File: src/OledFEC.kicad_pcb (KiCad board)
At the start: 2 copper layers, 24 x 27.9 mm, 14 parts, among them J1 105444-0001, J2 B4B-XH-A, U1 16F1454, U2 MIC2005A-1

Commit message: Using MIC2091-1 instead of MIC2005A-1
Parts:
- U2: footprint Medo64:U LoadSwitch 500mA [MIC2005A-1] (SOT23-5) -> Medo64:U LoadSwitch 100mA [MIC2091-1] (SOT23-5)
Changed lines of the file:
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@@
 		)
 	)
-	(footprint "Medo64:U LoadSwitch 500mA [MIC2005A-1] (SOT23-5)"
+	(footprint "Medo64:U LoadSwitch 100mA [MIC2091-1] (SOT23-5)"
 		(layer "F.Cu")
 		(at 28.2 36 -90)
 		(tags "SOT95P240X110-3N")
 		(property "Reference" "U2"
-			(at -2.8 0 0)
+			(at 0 -2.2 -90)
 			(layer "F.SilkS")
 			(effects
@@
 			)
 		)
-		(property "Footprint" "Medo64:U LoadSwitch 500mA [MIC2005A-1] (SOT23-5)"
-			(at 0 0 90)
+		(property "Footprint" "Medo64:U LoadSwitch 100mA [MIC2091-1] (SOT23-5)"
+			(at 0 0 -90)
 			(layer "F.Fab")
 			(hide yes)
@@
 		)
 		(property "Datasheet" ""
-			(at 0 0 90)
+			(at 0 0 -90)
 			(layer "F.Fab")
 			(hide yes)
@@
 		)
 		(property "Description" ""
-			(at 0 0 90)
+			(at 0 0 -90)
 			(layer "F.Fab")
 			(hide yes)
@@
 			(layer "F.Fab")
 		)
-		(fp_text user "~{FAULT}"
-			(at 0.7 0.95 90)
+		(fp_text user "EN"
+			(at -0.7 0.95 -90)
+			(layer "Cmts.User" knockout)
+			(effects
+				(font
+					(size 0.13 0.07)
+					(thickness 0.01)
+					(bold yes)
+				)
+				(justify left)
+			)
+		)
+		(fp_text user "IN"
+			(at -0.7 -0.95 -90)
+			(layer "Cmts.User" knockout)
+			(effects
+				(font
+					(size 0.13 0.07)
+					(thickness 0.01)
+					(bold yes)
+				)
+				(justify left)
+			)
+		)
+		(fp_text user "GND"
+			(at -0.7 0 -90)
 			(layer "Cmts.User" knockout)
 			(effects
@@
 		)
 		(fp_text user "OUT"
-			(at 0.7 -0.95 90)
-			(layer "Cmts.User" knockout)
-			(effects
-				(font
-					(size 0.13 0.07)
-					(thickness 0.01)
-					(bold yes)
-				)
-				(justify left)
-			)
-		)
-		(fp_text user "IN"
-			(at -0.7 -0.95 90)
+			(at 0.7 -0.95 -90)
 			(layer "Cmts.User" knockout)
 			(effects
@@
 			)
 		)
-		(fp_text user "EN"
-			(at -0.7 0.95 90)
+		(fp_text user "~{FAULT}"
+			(at 0.7 0.95 -90)
 			(layer "Cmts.User" knockout)
 			(effects
-				(font
-					(size 0.13 0.07)
-					(thickness 0.01)
-					(bold yes)
-				)
-				(justify right)
-			)
-		)
-		(fp_text user "GND"
-			(at -0.7 0 90)
-			(layer "Cmts.User" knockout)
-			(effects

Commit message: Cleanup
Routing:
- net 5V: track 47.6 -> 47.0 mm
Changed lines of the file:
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@@
-	)
-	(segment
-		(start 28.2 40.75)
-		(end 28.25 40.8)
-		(width 0.2)
-		(layer "F.Cu")
-		(net 4)
 	)
 	(segment
@@
 	)
 	(segment
-		(start 31.025 32.375)
-		(end 31.025 31.9)
-		(width 0.2)
-		(layer "F.Cu")
-		(net 6)
-	)
-	(segment
 		(start 29.15 33.65)
 		(end 29.15 34.75)
@@
 		(net 6)
 	)
-	(segment
-		(start 31.35 34.75)
-		(end 31.4 34.8)
-		(width 0.2)
-		(layer "F.Cu")
-		(net 6)
-	)
 	(via
 		(at 29.8 29.9)
@@
 		(width 0.2)
 		(layer "F.Cu")
-		(net 13)
-	)
-	(segment
-		(start 29.15 37.35)
-		(end 29.15 37.25)
-		(width 0.2)
-		(layer "F.Cu")

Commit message: Added pull-up jumper
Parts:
- added JP1: Jumper, Medo64:JP Dual (1205), F.Cu at (39.7, 44.9)
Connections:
- R3 pad 2: 3V3 -> PULL_UP
- R4 pad 2: 3V3 -> PULL_UP
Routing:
- net PULL_UP: track 0.00 -> 20.9 mm, vias 0 -> 3
- net 5V: track 47.0 -> 64.8 mm
- net OLED_SCL: track 32.1 -> 23.4 mm, vias 1 -> 2
- net 3V3: track 28.1 -> 34.3 mm, vias 5 -> 4
- net GND: track 82.7 -> 87.8 mm, vias 4 -> 5
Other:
- board text added: "3V3"
- board text added: "5V"

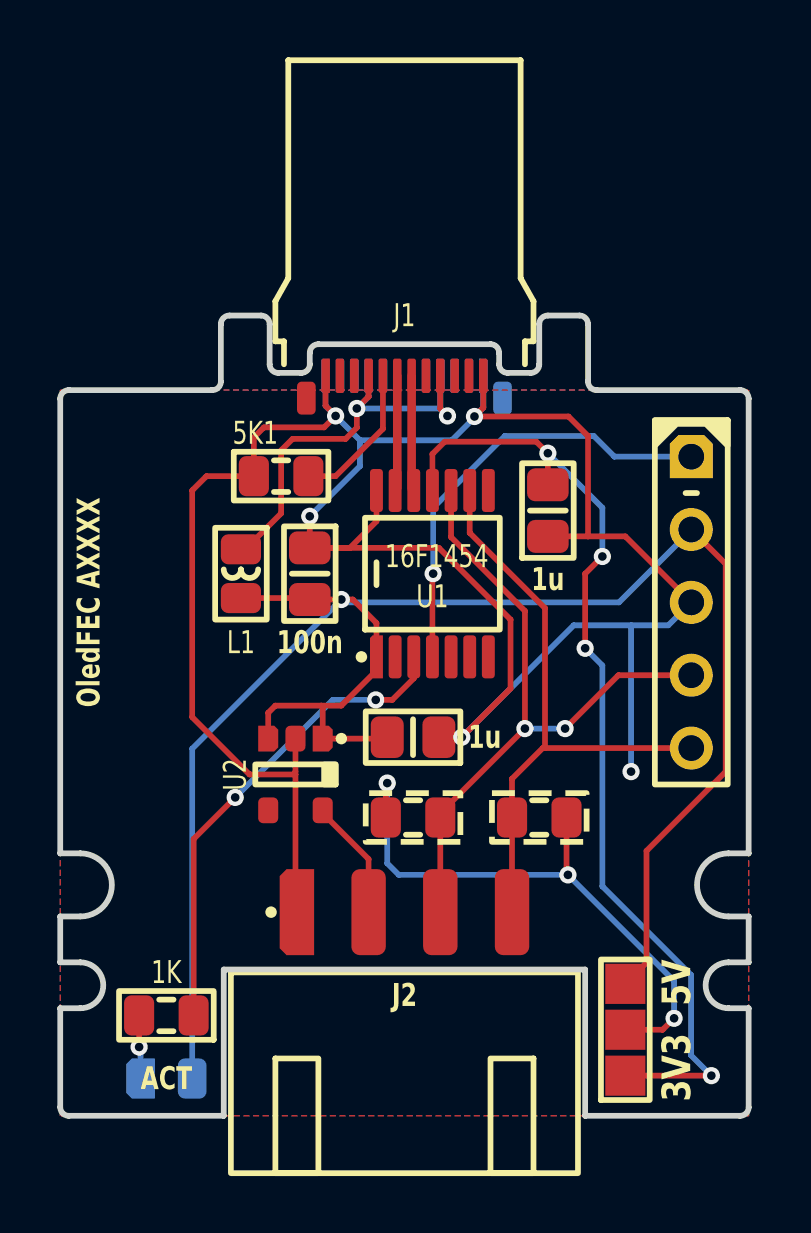
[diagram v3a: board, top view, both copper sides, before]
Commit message: Updated pull-up resistors to be populated
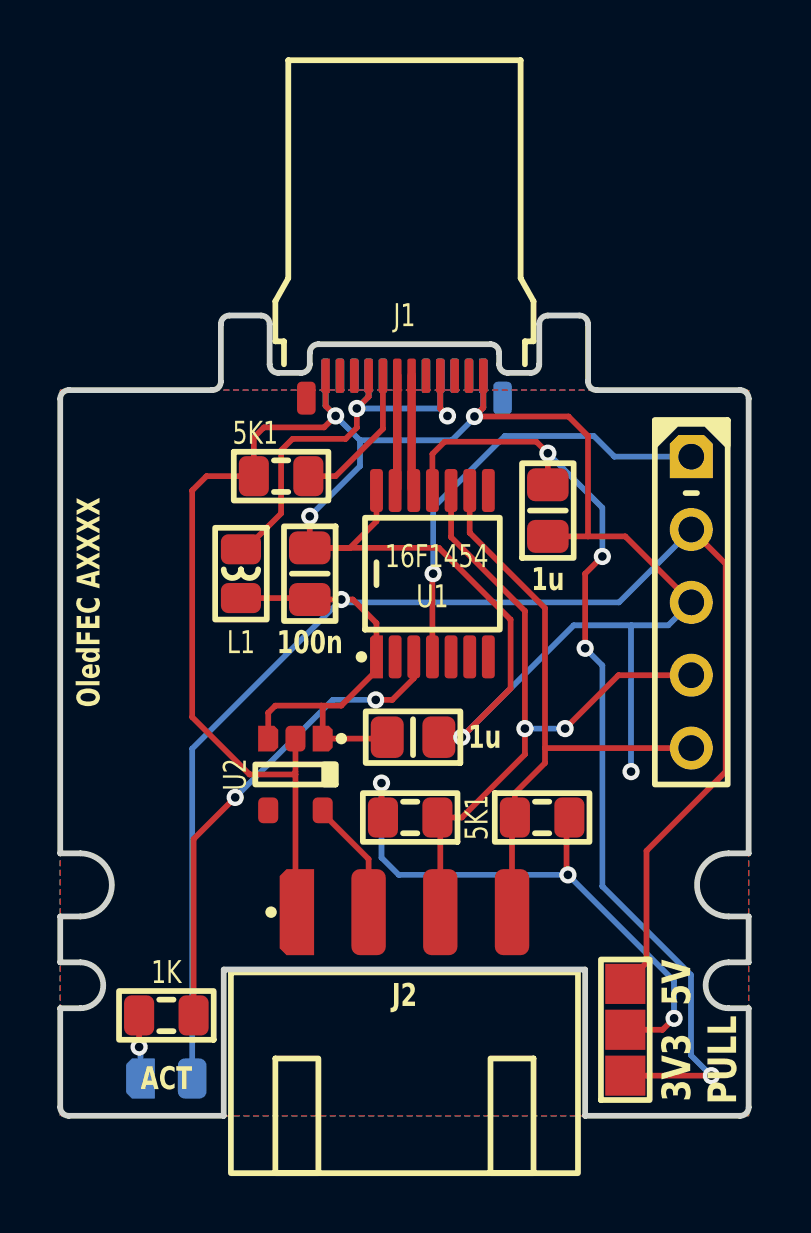
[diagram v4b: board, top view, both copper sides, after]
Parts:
- R3, R4: footprint Medo64:R Optional (0805) -> Medo64:R (0805)
- moved R3 0.10 mm to (32.2, 37.5)
- moved R4 0.10 mm to (36.8, 37.5)
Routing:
- net OLED_SCL: track 23.4 -> 24.1 mm
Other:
- board text added: "PULL"
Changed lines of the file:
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@@
 		)
 	)
-	(footprint "Medo64:R Optional (0805)"
+	(footprint "Medo64:R (0805)"
 		(layer "F.Cu")
-		(at 36.7 37.5)
+		(at 36.8 37.5)
 		(tags "RESC2013X70N")
 		(property "Reference" "R4"
@@
 			)
 		)
-		(property "Footprint" "Medo64:R Optional (0805)"
+		(property "Footprint" "Medo64:R (0805)"
 			(at 0 0 0)
-			(layer "B.Fab")
+			(layer "F.Fab")
 			(hide yes)
 			(effects
@@
 					(thickness 0.15)
 				)
-				(justify mirror)
 			)
 		)
 		(property "Datasheet" ""
 			(at 0 0 0)
-			(layer "B.Fab")
+			(layer "F.Fab")
 			(hide yes)
 			(effects
@@
 					(thickness 0.15)
 				)
-				(justify mirror)
 			)
 		)
 		(property "Description" ""
 			(at 0 0 0)
-			(layer "B.Fab")
+			(layer "F.Fab")
 			(hide yes)
 			(effects
@@
 					(thickness 0.15)
 				)
-				(justify mirror)
 			)
 		)
-		(attr smd exclude_from_bom)
+		(attr smd)
 		(fp_line
-			(start -0.25 -0.6)
-			(end 0.25 -0.6)
+			(start -0.25 -0.55)
+			(end 0.25 -0.55)
 			(stroke
 				(width 0.2)
@@
 		)
 		(fp_line
-			(start -0.25 0.6)
-			(end 0.25 0.6)
+			(start -0.25 0.55)
+			(end 0.25 0.55)
 			(stroke
 				(width 0.2)
@@
 			(stroke
 				(width 0.2)
-				(type dash)
+				(type default)
 			)
 			(fill none)
@@
 			(at -0.95 0)
 			(size 1.05 1.4)
-			(layers "F.Cu" "F.Mask")
+			(layers "F.Cu" "F.Paste" "F.Mask")
 			(roundrect_rratio 0.25)
 			(net 9 "OLED_SDA")
@@
 			(at 0.95 0)
 			(size 1.05 1.4)
-			(layers "F.Cu" "F.Mask")
+			(layers "F.Cu" "F.Paste" "F.Mask")
 			(roundrect_rratio 0.25)
 			(net 14 "PULL_UP")
 			(thermal_bridge_angle 45)
 		)
+		(model "${KICAD8_3DMODEL_DIR}/Resistor_SMD.3dshapes/R_0805_2012Metric.wrl"
+			(offset
+				(xyz 0 0 0)
+			)
+			(scale
+				(xyz 1 1 1)
+			)
+			(rotate
+				(xyz 0 0 0)
+			)
+		)
 	)
 	(footprint "Medo64:C (0805)"
@@
 		)
 	)
-	(footprint "Medo64:R Optional (0805)"
+	(footprint "Medo64:R (0805)"
 		(layer "F.Cu")
-		(at 32.3 37.5 180)
+		(at 32.2 37.5 180)
 		(tags "RESC2013X70N")
 		(property "Reference" "R3"
-			(at 0 -1.6 0)
+			(at 0 -1.6 180)
 			(layer "F.SilkS")
 			(hide yes)
@@
 		)
 		(property "Value" "5K1"
-			(at 0 1.7 0)
+			(at -2.325 0 90)
 			(layer "F.SilkS")
-			(hide yes)
 			(effects
 				(font
@@
 			)
 		)
-		(property "Footprint" "Medo64:R Optional (0805)"
-			(at 0 0 0)
-			(layer "B.Fab")
+		(property "Footprint" "Medo64:R (0805)"
+			(at 0 0 180)
+			(layer "F.Fab")
 			(hide yes)
 			(effects
@@
 					(thickness 0.15)
 				)
-				(justify mirror)
 			)
 		)
 		(property "Datasheet" ""
-			(at 0 0 0)
-			(layer "B.Fab")
+			(at 0 0 180)
+			(layer "F.Fab")
 			(hide yes)
 			(effects
@@
 					(thickness 0.15)
 				)
-				(justify mirror)
 			)
 		)
 		(property "Description" ""
-			(at 0 0 0)
-			(layer "B.Fab")
+			(at 0 0 180)
+			(layer "F.Fab")
 			(hide yes)
 			(effects
@@
 					(thickness 0.15)
 				)
-				(justify mirror)
 			)
 		)
-		(attr smd exclude_from_bom)
+		(attr smd)
 		(fp_line
-			(start -0.25 0.6)
-			(end 0.25 0.6)
+			(start -0.25 0.55)
+			(end 0.25 0.55)
 			(stroke
 				(width 0.2)
@@
 		)
 		(fp_line
-			(start -0.25 -0.6)
-			(end 0.25 -0.6)
+			(start -0.25 -0.55)
+			(end 0.25 -0.55)
 			(stroke
 				(width 0.2)
@@
 			(stroke
 				(width 0.2)
-				(type dash)
+				(type default)
 			)
 			(fill none)
@@
 			(at -0.95 0 180)
 			(size 1.05 1.4)
-			(layers "F.Cu" "F.Mask")
+			(layers "F.Cu" "F.Paste" "F.Mask")
 			(roundrect_rratio 0.25)
 			(net 8 "OLED_SCL")
@@
 			(at 0.95 0 180)
 			(size 1.05 1.4)
-			(layers "F.Cu" "F.Mask")
+			(layers "F.Cu" "F.Paste" "F.Mask")
 			(roundrect_rratio 0.25)
 			(net 14 "PULL_UP")
 			(thermal_bridge_angle 45)
 		)
+		(model "${KICAD8_3DMODEL_DIR}/Resistor_SMD.3dshapes/R_0805_2012Metric.wrl"
+			(offset
+				(xyz 0 0 0)
+			)
+			(scale
+				(xyz 1 1 1)
+			)
+			(rotate
+				(xyz 0 0 0)
+			)
+		)
 	)
 	(footprint "Medo64:U LoadSwitch 100mA [MIC2091-1] (SOT23-5)"
@@
 		)
 	)
+	(gr_text "PULL"
+		(at 43.1 45.95 90)
+		(layer "F.SilkS" knockout)
+		(effects
+			(font
+				(size 1 0.8)
+				(thickness 0.2)
+				(bold yes)
+			)
+		)
+	)
 	(segment
 		(start 31.25 23.95)
@@
 	)
 	(segment
+		(start 33.25 37.6)
+		(end 33.25 40.8)
+		(width 0.2)
+		(layer "F.Cu")
+		(net 8)
+	)
+	(segment
+		(start 33.15 37.5)
+		(end 33.25 37.6)
+		(width 0.2)
+		(layer "F.Cu")
+		(net 8)
+	)
+	(segment
+		(start 36.2 34.4)
+		(end 36.2 35.3)
+		(width 0.2)
+		(layer "F.Cu")
+		(net 8)
+	)
+	(segment
 		(start 42 32.54)
 		(end 39.46 32.54)
@@
 	)
 	(segment
-		(start 36.2 34.4)
-		(end 33.25 37.35)
+		(start 34 37.5)
+		(end 33.15 37.5)
 		(width 0.2)
 		(layer "F.Cu")
@@
 	)
 	(segment
-		(start 33.25 37.5)
-		(end 33.25 40.8)
+		(start 36.2 35.3)
+		(end 34 37.5)
 		(width 0.2)
 		(layer "F.Cu")
@@
 	)
 	(segment
-		(start 35.75 36.15)
-		(end 35.75 37.5)
+		(start 35.75 37.6)
+		(end 35.75 40.8)
 		(width 0.2)
 		(layer "F.Cu")
@@
 	)
 	(segment
-		(start 35.75 37.5)
-		(end 35.75 40.8)
+		(start 35.85 36.65)
+		(end 35.85 37.5)
 		(width 0.2)
 		(layer "F.Cu")
@@
 	)
 	(segment
-		(start 36.9 30.2)
-		(end 36.9 35.08)
+		(start 35.85 37.5)
+		(end 35.75 37.6)
+		(width 0.2)
+		(layer "F.Cu")
+		(net 9)
+	)
+	(segment
+		(start 36.9 35.6)
+		(end 35.85 36.65)
 		(width 0.2)
 		(layer "F.Cu")
@@
 	(segment
 		(start 36.9 35.08)
-		(end 36.82 35.08)
+		(end 36.9 35.6)
 		(width 0.2)
 		(layer "F.Cu")
@@
 	)
 	(segment
-		(start 34.275 27.575)
-		(end 36.9 30.2)
+		(start 36.9 30.2)
+		(end 36.9 35.08)
 		(width 0.2)
 		(layer "F.Cu")
@@
 	)
 	(segment
-		(start 34.275 26.1)
-		(end 34.275 27.575)
+		(start 34.275 27.575)
+		(end 36.9 30.2)
 		(width 0.2)
 		(layer "F.Cu")
@@
 	)
 	(segment
-		(start 36.82 35.08)
-		(end 35.75 36.15)
+		(start 34.275 26.1)
+		(end 34.275 27.575)
 		(width 0.2)
 		(layer "F.Cu")
@@
 	)
 	(segment
+		(start 31.2 37.35)
+		(end 31.2 36.300006)
+		(width 0.2)
+		(layer "F.Cu")
+		(net 14)
+	)
+	(segment
 		(start 41 44.9)
 		(end 41.4 44.5)
@@
 	(segment
 		(start 31.35 37.5)
-		(end 31.35 36.35)
+		(end 31.2 37.35)
 		(width 0.2)
 		(layer "F.Cu")
@@
 	)
 	(segment
-		(start 31.35 36.35)
-		(end 31.4 36.3)
+		(start 31.2 36.300006)
+		(end 31.199994 36.3)
 		(width 0.2)
 		(layer "F.Cu")
@@
 	)
 	(via
-		(at 31.4 36.3)
+		(at 31.199994 36.3)
 		(size 0.6)
 		(drill 0.3)
@@
 	)
 	(segment
-		(start 31.8 39.5)
-		(end 37.7 39.5)
+		(start 37.7 39.5)
+		(end 31.8 39.5)
 		(width 0.2)
 		(layer "B.Cu")
@@
 	)
 	(segment
-		(start 31.4 36.3)
-		(end 31.4 39.1)
+		(start 37.7 39.5)
+		(end 41.4 43.2)
 		(width 0.2)
 		(layer "B.Cu")
@@
 	)
 	(segment
-		(start 31.4 39.1)
-		(end 31.8 39.5)
+		(start 31.8 39.5)
+		(end 31.199994 38.899994)
 		(width 0.2)
 		(layer "B.Cu")
@@
 	)
 	(segment
-		(start 37.7 39.5)
-		(end 41.4 43.2)
+		(start 31.199994 38.899994)
+		(end 31.199994 36.3)
 		(width 0.2)
 		(layer "B.Cu")
